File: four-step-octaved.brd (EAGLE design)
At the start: 100 x 80 mm, 36 parts, among them IC1 556, IC2 4017N, IC3 4040N, J1 BATTERY, J2 SPEAKER, U1 LM386N

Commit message: Tidier board
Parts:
- moved J1 100.2 mm to (88.3, 21.0), turned to 90 degrees
- moved RV1 67.7 mm to (87.0, 3.17)
- moved R1 57.6 mm to (85.7, 12.1)
- moved C3 27.0 mm to (45.1, 26.7), turned to 270 degrees
- moved R3 24.8 mm to (41.3, 26.7), turned to 270 degrees
- moved C6 21.6 mm to (87.6, 36.8), turned to 180 degrees
- moved IC3 21.1 mm to (59.7, 30.5)
- moved C5 21.0 mm to (67.3, 37.5), turned to 270 degrees
- moved RV5 21.0 mm to (66.7, 3.17)
- moved RV6 20.7 mm to (79.4, 3.17)
- moved C2 20.2 mm to (41.3, 36.2), turned to 270 degrees
- moved J2 19.7 mm to (88.3, 27.3), turned to 90 degrees
- moved R4 19.3 mm to (15.2, 27.9), turned to 90 degrees
- moved RV4 19.3 mm to (48.3, 3.17)
- moved RV3 18.1 mm to (29.8, 3.17)
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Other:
- board size 100 x 80 mm -> 93.7 x 43.2 mm

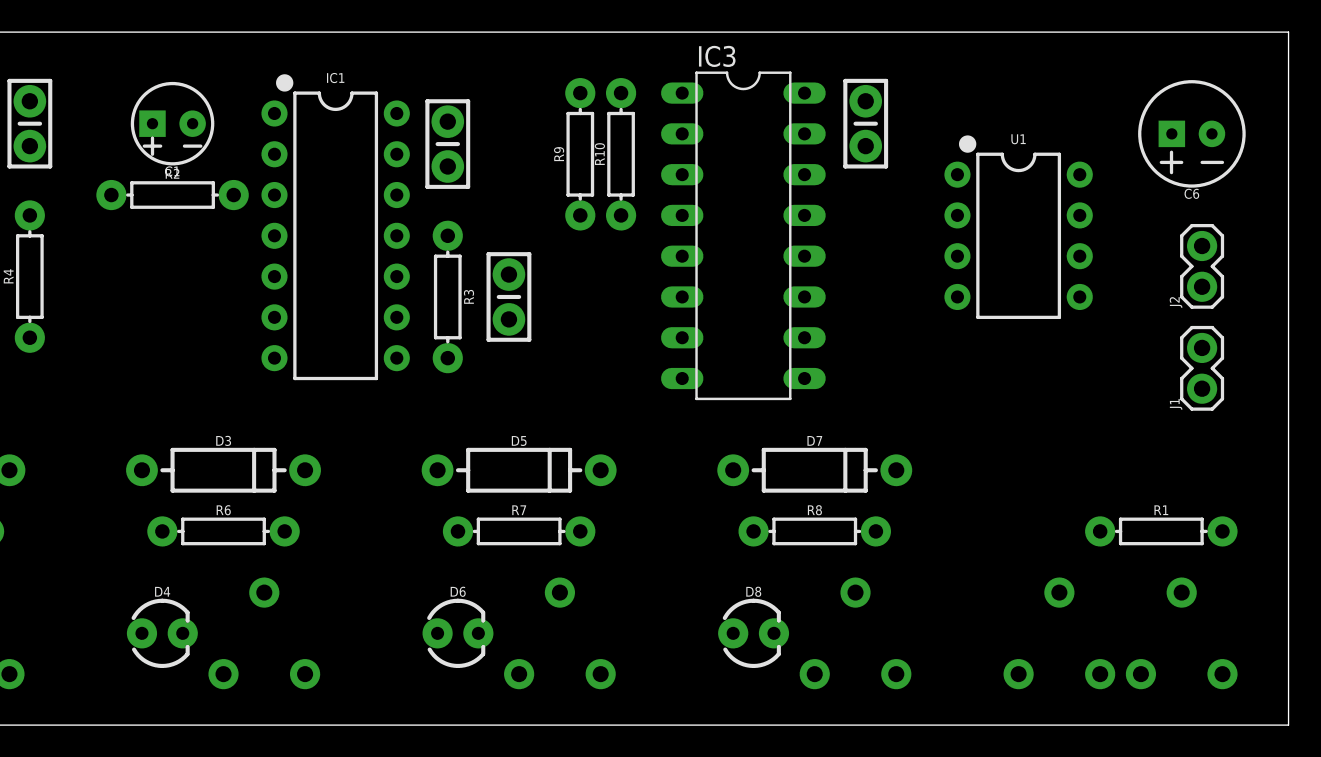
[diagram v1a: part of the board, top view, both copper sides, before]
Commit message: Add board text and cleanup
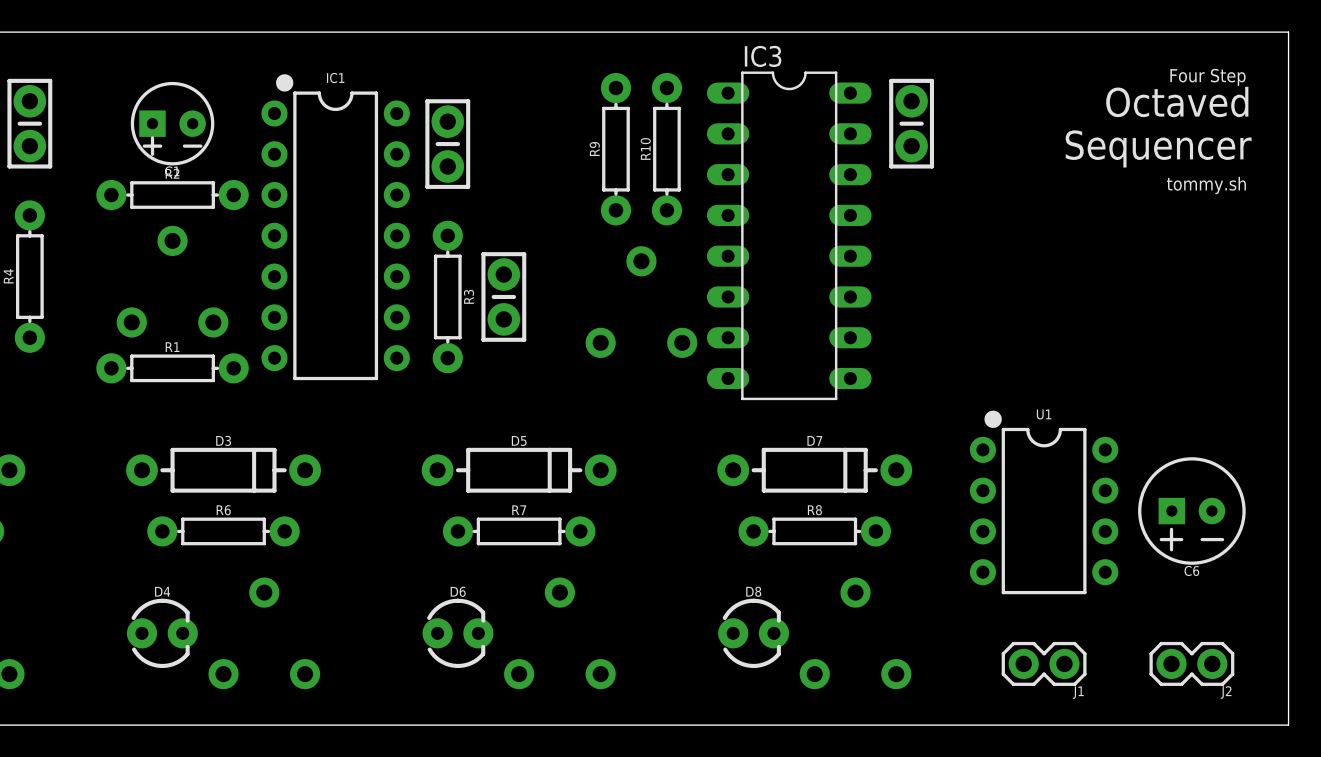
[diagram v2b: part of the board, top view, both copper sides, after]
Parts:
- moved RV1 66.6 mm to (24.1, 25.1)
- moved R1 62.4 mm to (24.1, 22.2)
- moved RV6 33.2 mm to (53.3, 23.8)
- moved J2 23.5 mm to (88.9, 3.81), turned to 180 degrees
- moved C6 23.5 mm to (87.6, 13.3)
- moved J1 19.2 mm to (79.7, 3.81), turned to 180 degrees
- moved U1 17.2 mm to (78.4, 13.3)
- moved R10 2.88 mm to (54.9, 35.9)
- moved C5 2.86 mm to (70.2, 37.5)
- moved IC3 2.86 mm to (62.5, 30.5)
- moved R9 2.25 mm to (51.8, 35.9)
- moved C3 0.32 mm to (44.8, 26.7)
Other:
- board text added: "Four Step"
- board text added: "Octaved Sequencer"
- board text added: "tommy.sh"

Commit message: Shorten schematic to fit on one page
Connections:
- net GND: now also R4.P$2; no longer R4.P$1
- net N$5: now also R4.P$1; no longer R4.P$2
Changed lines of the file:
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@@
 <contactref element="RV1" pad="1"/>
 <contactref element="R2" pad="P$1"/>
+<wire x1="24.13" y1="30.1625" x2="30.48" y2="38.1" width="0" layer="19" extent="1-1"/>
+<wire x1="20.32" y1="33.02" x2="24.13" y2="30.1625" width="0" layer="19" extent="1-1"/>
 <wire x1="21.59" y1="25.0825" x2="24.13" y2="30.1625" width="0" layer="19" extent="1-1"/>
-<wire x1="30.48" y1="38.1" x2="24.13" y2="30.1625" width="0" layer="19" extent="1-1"/>
-<wire x1="20.32" y1="33.02" x2="30.48" y2="38.1" width="0" layer="19" extent="1-1"/>
 </signal>
 <signal name="+9V">
 <contactref element="R1" pad="P$1"/>
+<contactref element="J1" pad="1"/>
 <contactref element="IC1" pad="4"/>
 <contactref element="IC1" pad="14"/>
@@
 <contactref element="IC2" pad="16"/>
 <contactref element="C4" pad="1"/>
+<contactref element="U1" pad="6"/>
 <contactref element="IC3" pad="16"/>
 <contactref element="C5" pad="1"/>
-<contactref element="U1" pad="6"/>
-<contactref element="J1" pad="1"/>
-<wire x1="79.6925" y1="3.81" x2="82.2325" y2="12.065" width="0" layer="19" extent="1-1"/>
-<wire x1="20.32" y1="22.225" x2="79.6925" y2="3.81" width="0" layer="19" extent="1-1"/>
-<wire x1="70.1675" y1="38.862" x2="82.2325" y2="12.065" width="0" layer="19" extent="1-1"/>
 <wire x1="66.3575" y1="39.37" x2="70.1675" y2="38.862" width="0" layer="19" extent="1-1"/>
 <wire x1="41.275" y1="37.592" x2="66.3575" y2="39.37" width="0" layer="19" extent="1-1"/>
 <wire x1="38.1" y1="38.1" x2="41.275" y2="37.592" width="0" layer="19" extent="1-1"/>
 <wire x1="30.48" y1="30.48" x2="38.1" y2="38.1" width="0" layer="19" extent="1-1"/>
+<wire x1="20.32" y1="22.225" x2="30.48" y2="30.48" width="0" layer="19" extent="1-1"/>
 <wire x1="15.24" y1="38.862" x2="30.48" y2="30.48" width="0" layer="19" extent="1-1"/>
 <wire x1="11.43" y1="39.37" x2="15.24" y2="38.862" width="0" layer="19" extent="1-1"/>
+<wire x1="82.2325" y1="12.065" x2="70.1675" y2="38.862" width="0" layer="19" extent="1-1"/>
+<wire x1="79.6925" y1="3.81" x2="82.2325" y2="12.065" width="0" layer="19" extent="1-1"/>
 </signal>
 <signal name="N$3">
@@
 <contactref element="IC1" pad="5"/>
 <contactref element="IC2" pad="14"/>
-<contactref element="R4" pad="P$2"/>
-<wire x1="15.24" y1="31.75" x2="30.48" y2="27.94" width="0" layer="19" extent="1-1"/>
-<wire x1="11.43" y1="34.29" x2="15.24" y2="31.75" width="0" layer="19" extent="1-1"/>
+<contactref element="R4" pad="P$1"/>
+<wire x1="15.24" y1="24.13" x2="30.48" y2="27.94" width="0" layer="19" extent="1-1"/>
+<wire x1="11.43" y1="34.29" x2="15.24" y2="24.13" width="0" layer="19" extent="1-1"/>
 </signal>
 <signal name="N$9">
@@
 <wire x1="11.43" y1="24.13" x2="11.43" y2="36.83" width="0" layer="19" extent="1-1"/>
 </signal>
-<signal name="N$21">
-<contactref element="IC3" pad="10"/>
-<contactref element="IC1" pad="9"/>
-<wire x1="38.1" y1="25.4" x2="66.3575" y2="24.13" width="0" layer="19" extent="1-1"/>
-</signal>
 <signal name="N$22">
 <contactref element="R10" pad="P$2"/>
@@
 <contactref element="R10" pad="P$1"/>
 <contactref element="RV6" pad="3"/>
-<wire x1="54.9275" y1="32.0675" x2="55.88" y2="23.8125" width="0" layer="19" extent="1-1"/>
 <wire x1="51.7525" y1="32.0675" x2="54.9275" y2="32.0675" width="0" layer="19" extent="1-1"/>
+<wire x1="55.88" y1="23.8125" x2="54.9275" y2="32.0675" width="0" layer="19" extent="1-1"/>
 </signal>
 <signal name="N$20">
@@
 <wire x1="82.2325" y1="9.525" x2="86.38" y2="13.335" width="0" layer="19" extent="1-1"/>
 </signal>
+<signal name="N$43">
+<contactref element="IC3" pad="10"/>
+<contactref element="IC1" pad="9"/>
+<wire x1="38.1" y1="25.4" x2="66.3575" y2="24.13" width="0" layer="19" extent="1-1"/>
+</signal>
 <signal name="GND">
-<contactref element="IC1" pad="7"/>
-<contactref element="R4" pad="P$1"/>
+<contactref element="C5" pad="2"/>
+<contactref element="IC3" pad="8"/>
+<contactref element="IC3" pad="11"/>
+<contactref element="RV6" pad="2"/>
+<contactref element="U1" pad="2"/>
+<contactref element="U1" pad="4"/>
+<contactref element="J2" pad="2"/>
 <contactref element="D2" pad="K"/>
 <contactref element="D4" pad="K"/>
 <contactref element="D6" pad="K"/>
 <contactref element="D8" pad="K"/>
+<contactref element="J1" pad="2"/>
+<contactref element="IC1" pad="7"/>
+<contactref element="C3" pad="2"/>
+<contactref element="C2" pad="2"/>
+<contactref element="IC2" pad="13"/>
 <contactref element="C4" pad="2"/>
 <contactref element="IC2" pad="8"/>
-<contactref element="IC2" pad="13"/>
+<contactref element="R4" pad="P$2"/>
 <contactref element="C1" pad="2"/>
-<contactref element="C3" pad="2"/>
-<contactref element="C2" pad="2"/>
-<contactref element="IC3" pad="11"/>
-<contactref element="C5" pad="2"/>
-<contactref element="IC3" pad="8"/>
-<contactref element="RV6" pad="2"/>
-<contactref element="J2" pad="2"/>
-<contactref element="U1" pad="4"/>
-<contactref element="U1" pad="2"/>
-<contactref element="J1" pad="2"/>
-<wire x1="77.1525" y1="3.81" x2="86.36" y2="3.81" width="0" layer="19" extent="1-1"/>
-<wire x1="74.6125" y1="14.605" x2="86.36" y2="3.81" width="0" layer="19" extent="1-1"/>
-<wire x1="74.6125" y1="9.525" x2="74.6125" y2="14.605" width="0" layer="19" extent="1-1"/>
-<wire x1="70.1675" y1="36.068" x2="74.6125" y2="14.605" width="0" layer="19" extent="1-1"/>
-<wire x1="66.3575" y1="26.67" x2="74.6125" y2="9.525" width="0" layer="19" extent="1-1"/>
+<wire x1="66.3575" y1="26.67" x2="70.1675" y2="36.068" width="0" layer="19" extent="1-1"/>
 <wire x1="58.7375" y1="21.59" x2="66.3575" y2="26.67" width="0" layer="19" extent="1-1"/>
-<wire x1="44.7675" y1="25.273" x2="58.7375" y2="21.59" width="0" layer="19" extent="1-1"/>
+<wire x1="50.8" y1="23.8125" x2="58.7375" y2="21.59" width="0" layer="19" extent="1-1"/>
+<wire x1="44.7675" y1="25.273" x2="50.8" y2="23.8125" width="0" layer="19" extent="1-1"/>
 <wire x1="41.275" y1="34.798" x2="44.7675" y2="25.273" width="0" layer="19" extent="1-1"/>
 <wire x1="30.48" y1="22.86" x2="44.7675" y2="25.273" width="0" layer="19" extent="1-1"/>
-<wire x1="15.24" y1="24.13" x2="30.48" y2="22.86" width="0" layer="19" extent="1-1"/>
-<wire x1="11.43" y1="31.75" x2="15.24" y2="24.13" width="0" layer="19" extent="1-1"/>
-<wire x1="15.24" y1="36.068" x2="11.43" y2="31.75" width="0" layer="19" extent="1-1"/>
-<wire x1="25.38" y1="37.465" x2="15.24" y2="36.068" width="0" layer="19" extent="1-1"/>
-<wire x1="3.81" y1="21.59" x2="15.24" y2="24.13" width="0" layer="19" extent="1-1"/>
+<wire x1="74.6125" y1="14.605" x2="66.3575" y2="26.67" width="0" layer="19" extent="1-1"/>
+<wire x1="74.6125" y1="9.525" x2="74.6125" y2="14.605" width="0" layer="19" extent="1-1"/>
+<wire x1="77.1525" y1="3.81" x2="74.6125" y2="9.525" width="0" layer="19" extent="1-1"/>
+<wire x1="86.36" y1="3.81" x2="77.1525" y2="3.81" width="0" layer="19" extent="1-1"/>
+<wire x1="61.595" y1="5.715" x2="74.6125" y2="9.525" width="0" layer="19" extent="1-1"/>
+<wire x1="25.38" y1="37.465" x2="30.48" y2="22.86" width="0" layer="19" extent="1-1"/>
+<wire x1="15.24" y1="36.068" x2="25.38" y2="37.465" width="0" layer="19" extent="1-1"/>
+<wire x1="15.24" y1="31.75" x2="15.24" y2="36.068" width="0" layer="19" extent="1-1"/>
+<wire x1="11.43" y1="31.75" x2="15.24" y2="31.75" width="0" layer="19" extent="1-1"/>
+<wire x1="3.81" y1="21.59" x2="11.43" y2="31.75" width="0" layer="19" extent="1-1"/>
 <wire x1="5.715" y1="5.715" x2="3.81" y2="21.59" width="0" layer="19" extent="1-1"/>
-<wire x1="61.595" y1="5.715" x2="58.7375" y2="21.59" width="0" layer="19" extent="1-1"/>
-<wire x1="50.8" y1="23.8125" x2="61.595" y2="5.715" width="0" layer="19" extent="1-1"/>
 <wire x1="24.765" y1="5.715" x2="30.48" y2="22.86" width="0" layer="19" extent="1-1"/>
 <wire x1="43.18" y1="5.715" x2="61.595" y2="5.715" width="0" layer="19" extent="1-1"/>

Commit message: Clean up board text
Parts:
- moved RV1 50.8 mm to (74.9, 24.1)
- moved RV6 31.4 mm to (84.8, 24.1)
- moved R1 6.98 mm to (24.1, 29.2)
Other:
- board text added: "C2"
- board text added: "C3"
- board text added: "C4"
- board text added: "C5"
- board text added: "Four Step Octaved Sequencer"
- board text added: "RV1"
- board text added: "RV6"
- board text added: "TEMPO"
- board text added: "VOLUME"
- board text removed: "Four Step"
- board text removed: "Octaved Sequencer"
